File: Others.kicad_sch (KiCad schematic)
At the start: 18 parts, among them J15 UFL, J16 IO1, J17 IO2, Q14 SI2312BDS

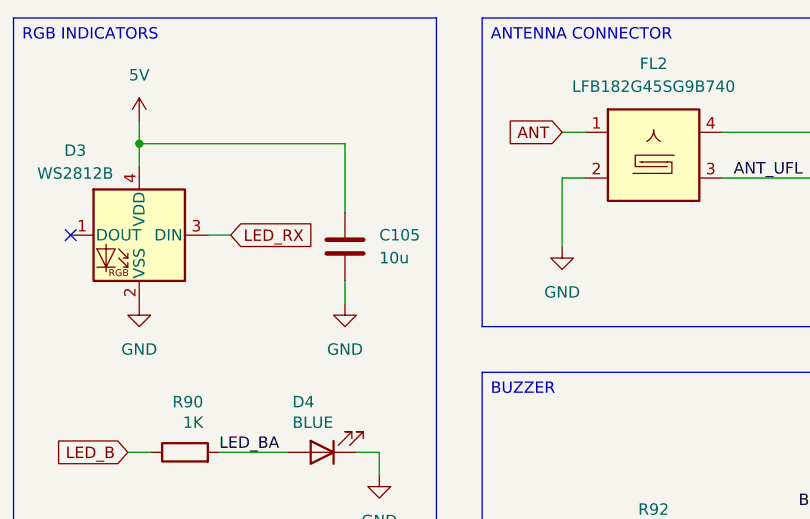
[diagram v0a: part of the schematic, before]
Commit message: Oscillator and IMU layout
Updated the oscillator layout for the RP2350.
Updated the IMU layout for the IMU.
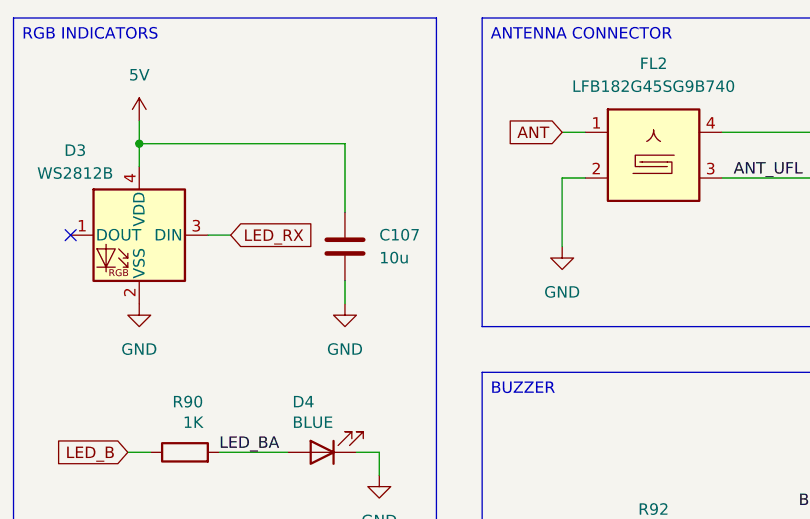
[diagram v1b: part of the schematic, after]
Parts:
- renumbered C105 to C107
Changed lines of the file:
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@@
 		(on_board yes)
 		(dnp no)
-		(property "Reference" "#PWR0216"
+		(property "Reference" "#PWR0217"
 			(at 111.76 96.52 0)
 			(effects
@@
 			(project "ThunderHorse"
 				(path "/ac187c6c-fa53-41cc-bce1-6f39a42a92e8/111cf19a-e0f8-4ba5-b5cb-1102d2b05aed"
-					(reference "#PWR0216")
+					(reference "#PWR0217")
 					(unit 1)
 				)
@@
 		(dnp no)
 		(fields_autoplaced yes)
-		(property "Reference" "#PWR0219"
+		(property "Reference" "#PWR0220"
 			(at 151.13 116.84 0)
 			(effects
@@
 			(project "ThunderHorse"
 				(path "/ac187c6c-fa53-41cc-bce1-6f39a42a92e8/111cf19a-e0f8-4ba5-b5cb-1102d2b05aed"
-					(reference "#PWR0219")
+					(reference "#PWR0220")
 					(unit 1)
 				)
@@
 		(dnp no)
 		(fields_autoplaced yes)
-		(property "Reference" "#PWR0214"
+		(property "Reference" "#PWR0215"
 			(at 85.09 77.47 0)
 			(effects
@@
 			(project "ThunderHorse"
 				(path "/ac187c6c-fa53-41cc-bce1-6f39a42a92e8/111cf19a-e0f8-4ba5-b5cb-1102d2b05aed"
-					(reference "#PWR0214")
+					(reference "#PWR0215")
 					(unit 1)
 				)
@@
 		(dnp no)
 		(fields_autoplaced yes)
-		(property "Reference" "#PWR0222"
+		(property "Reference" "#PWR0223"
 			(at 165.1 71.12 0)
 			(effects
@@
 			(project "ThunderHorse"
 				(path "/ac187c6c-fa53-41cc-bce1-6f39a42a92e8/111cf19a-e0f8-4ba5-b5cb-1102d2b05aed"
-					(reference "#PWR0222")
+					(reference "#PWR0223")
 					(unit 1)
 				)
@@
 		(dnp no)
 		(fields_autoplaced yes)
-		(property "Reference" "#PWR0228"
+		(property "Reference" "#PWR0229"
 			(at 217.17 57.15 0)
 			(effects
@@
 			(project "ThunderHorse"
 				(path "/ac187c6c-fa53-41cc-bce1-6f39a42a92e8/111cf19a-e0f8-4ba5-b5cb-1102d2b05aed"
-					(reference "#PWR0228")
+					(reference "#PWR0229")
 					(unit 1)
 				)
@@
 		(on_board yes)
 		(dnp no)
-		(property "Reference" "#PWR0217"
+		(property "Reference" "#PWR0218"
 			(at 111.76 114.3 0)
 			(effects
@@
 			(project "ThunderHorse"
 				(path "/ac187c6c-fa53-41cc-bce1-6f39a42a92e8/111cf19a-e0f8-4ba5-b5cb-1102d2b05aed"
-					(reference "#PWR0217")
+					(reference "#PWR0218")
 					(unit 1)
 				)
@@
 		(dnp no)
 		(fields_autoplaced yes)
-		(property "Reference" "#PWR0218"
+		(property "Reference" "#PWR0219"
 			(at 132.08 71.12 0)
 			(effects
@@
 			(project "ThunderHorse"
 				(path "/ac187c6c-fa53-41cc-bce1-6f39a42a92e8/111cf19a-e0f8-4ba5-b5cb-1102d2b05aed"
-					(reference "#PWR0218")
+					(reference "#PWR0219")
 					(unit 1)
 				)
@@
 		(on_board yes)
 		(dnp no)
-		(property "Reference" "#PWR0213"
+		(property "Reference" "#PWR0214"
 			(at 85.09 54.61 0)
 			(effects
@@
 			(project "ThunderHorse"
 				(path "/ac187c6c-fa53-41cc-bce1-6f39a42a92e8/111cf19a-e0f8-4ba5-b5cb-1102d2b05aed"
-					(reference "#PWR0213")
+					(reference "#PWR0214")
 					(unit 1)
 				)
@@
 		(dnp no)
 		(fields_autoplaced yes)
-		(property "Reference" "#PWR0223"
+		(property "Reference" "#PWR0224"
 			(at 173.99 71.12 0)
 			(effects
@@
 			(project "ThunderHorse"
 				(path "/ac187c6c-fa53-41cc-bce1-6f39a42a92e8/111cf19a-e0f8-4ba5-b5cb-1102d2b05aed"
-					(reference "#PWR0223")
+					(reference "#PWR0224")
 					(unit 1)
 				)
@@
 		(dnp no)
 		(fields_autoplaced yes)
-		(property "Reference" "#PWR0215"
+		(property "Reference" "#PWR0216"
 			(at 107.95 77.47 0)
 			(effects
@@
 			(project "ThunderHorse"
 				(path "/ac187c6c-fa53-41cc-bce1-6f39a42a92e8/111cf19a-e0f8-4ba5-b5cb-1102d2b05aed"
-					(reference "#PWR0215")
+					(reference "#PWR0216")
 					(unit 1)
 				)
@@
 		(dnp no)
 		(fields_autoplaced yes)
-		(property "Reference" "#PWR0226"
+		(property "Reference" "#PWR0227"
 			(at 213.36 92.71 0)
 			(effects
@@
 			(project "ThunderHorse"
 				(path "/ac187c6c-fa53-41cc-bce1-6f39a42a92e8/111cf19a-e0f8-4ba5-b5cb-1102d2b05aed"
-					(reference "#PWR0226")
+					(reference "#PWR0227")
 					(unit 1)
 				)
@@
 		(dnp no)
 		(fields_autoplaced yes)
-		(property "Reference" "#PWR0220"
+		(property "Reference" "#PWR0221"
 			(at 161.29 91.44 0)
 			(effects
@@
 			(project "ThunderHorse"
 				(path "/ac187c6c-fa53-41cc-bce1-6f39a42a92e8/111cf19a-e0f8-4ba5-b5cb-1102d2b05aed"
-					(reference "#PWR0220")
+					(reference "#PWR0221")
 					(unit 1)
 				)
@@
 		(dnp no)
 		(fields_autoplaced yes)
-		(property "Reference" "#PWR0229"
+		(property "Reference" "#PWR0230"
 			(at 217.17 92.71 0)
 			(effects
@@
 			(project "ThunderHorse"
 				(path "/ac187c6c-fa53-41cc-bce1-6f39a42a92e8/111cf19a-e0f8-4ba5-b5cb-1102d2b05aed"
-					(reference "#PWR0229")
+					(reference "#PWR0230")
 					(unit 1)
 				)
@@
 		(dnp no)
 		(fields_autoplaced yes)
-		(property "Reference" "C105"
+		(property "Reference" "C107"
 			(at 111.76 63.4999 0)
 			(effects
@@
 			(project "ThunderHorse"
 				(path "/ac187c6c-fa53-41cc-bce1-6f39a42a92e8/111cf19a-e0f8-4ba5-b5cb-1102d2b05aed"
-					(reference "C105")
+					(reference "C107")
 					(unit 1)
 				)
@@
 		(dnp no)
 		(fields_autoplaced yes)
-		(property "Reference" "#PWR0221"
+		(property "Reference" "#PWR0222"
 			(at 161.29 116.84 0)
 			(effects
@@
 			(project "ThunderHorse"
 				(path "/ac187c6c-fa53-41cc-bce1-6f39a42a92e8/111cf19a-e0f8-4ba5-b5cb-1102d2b05aed"
-					(reference "#PWR0221")
+					(reference "#PWR0222")
 					(unit 1)
 				)
@@
 		(dnp no)
 		(fields_autoplaced yes)
-		(property "Reference" "#PWR0227"
+		(property "Reference" "#PWR0228"
 			(at 213.36 113.03 0)
 			(effects
@@
 			(project "ThunderHorse"
 				(path "/ac187c6c-fa53-41cc-bce1-6f39a42a92e8/111cf19a-e0f8-4ba5-b5cb-1102d2b05aed"
-					(reference "#PWR0227")
+					(reference "#PWR0228")
 					(unit 1)
 				)
@@
 		(dnp no)
 		(fields_autoplaced yes)
-		(property "Reference" "#PWR0225"
+		(property "Reference" "#PWR0226"
 			(at 213.36 77.47 0)
 			(effects
@@
 			(project "ThunderHorse"
 				(path "/ac187c6c-fa53-41cc-bce1-6f39a42a92e8/111cf19a-e0f8-4ba5-b5cb-1102d2b05aed"
-					(reference "#PWR0225")
+					(reference "#PWR0226")
 					(unit 1)
 				)
@@
 		(dnp no)
 		(fields_autoplaced yes)
-		(property "Reference" "#PWR0224"
+		(property "Reference" "#PWR0225"
 			(at 213.36 57.15 0)
 			(effects
@@
 			(project "ThunderHorse"
 				(path "/ac187c6c-fa53-41cc-bce1-6f39a42a92e8/111cf19a-e0f8-4ba5-b5cb-1102d2b05aed"
-					(reference "#PWR0224")
-					(unit 1)
-				)
+					(reference "#PWR0225")
+					(unit 1)
+				)

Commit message: Power and ESC layout
Updated the power layout.
Updated the ESC layout.

TODO:
Improve track spacing for the ESC.
Complete the power connections.
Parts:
- D4, D5: footprint LED_SMD:LED_0805_2012Metric -> LED_SMD:LED_0603_1608Metric
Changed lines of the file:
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@@
 			)
 		)
-		(property "Footprint" "LED_SMD:LED_0805_2012Metric"
+		(property "Footprint" "LED_SMD:LED_0603_1608Metric"
 			(at 105.41 87.63 0)
 			(effects
@@
 			)
 		)
-		(property "Footprint" "LED_SMD:LED_0805_2012Metric"
+		(property "Footprint" "LED_SMD:LED_0603_1608Metric"
 			(at 105.41 105.41 0)
 			(effects

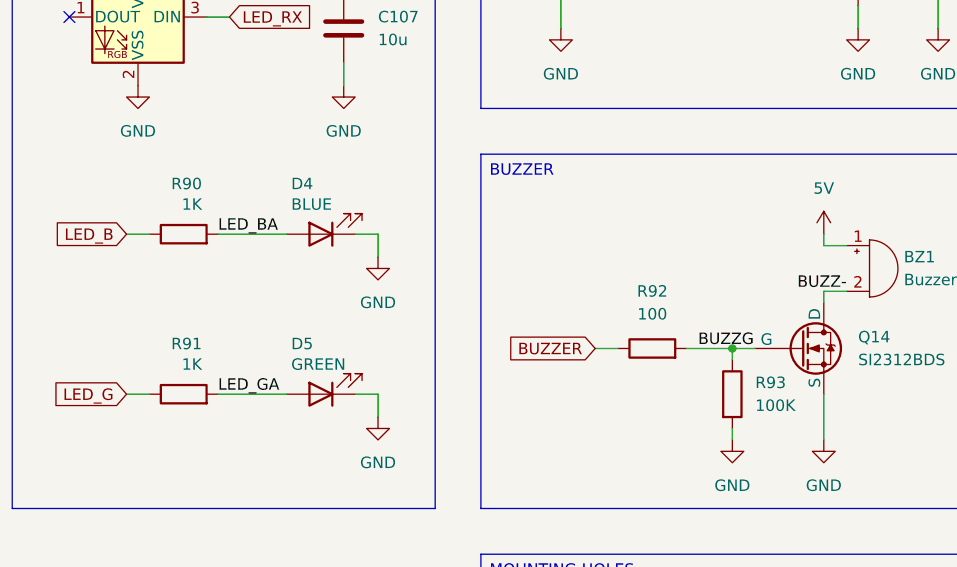
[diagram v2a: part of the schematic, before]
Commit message: Voltage detection
Added a VBUS voltage detection for the RP.
Minor layout changes.
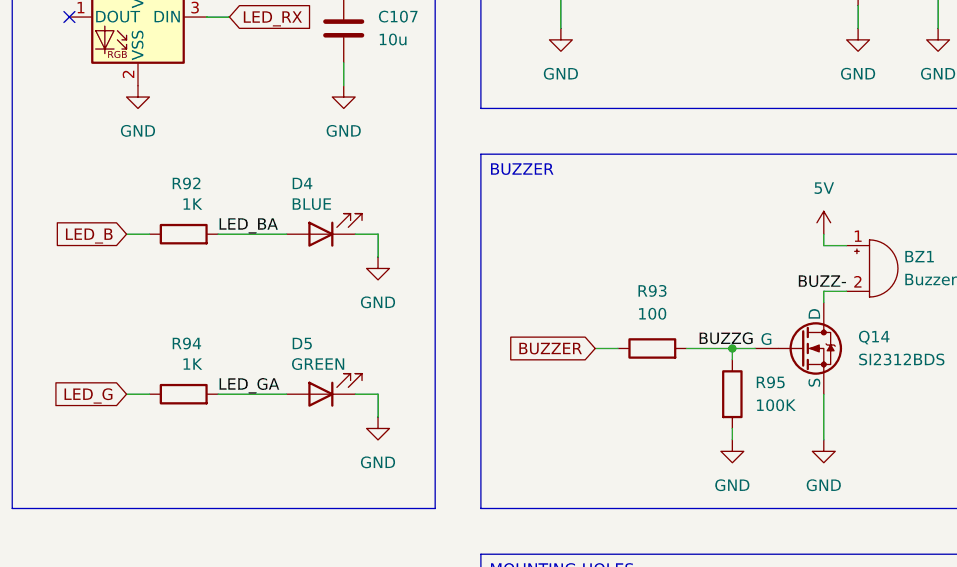
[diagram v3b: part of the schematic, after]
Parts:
- renumbered R90 to R92, R92 to R93, R91 to R94, R93 to R95
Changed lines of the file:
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@@
 		(on_board yes)
 		(dnp no)
-		(property "Reference" "#PWR0217"
+		(property "Reference" "#PWR0227"
 			(at 111.76 96.52 0)
 			(effects
@@
 			(project "ThunderHorse"
 				(path "/ac187c6c-fa53-41cc-bce1-6f39a42a92e8/111cf19a-e0f8-4ba5-b5cb-1102d2b05aed"
-					(reference "#PWR0217")
+					(reference "#PWR0227")
 					(unit 1)
 				)
@@
 		(dnp no)
 		(fields_autoplaced yes)
-		(property "Reference" "#PWR0220"
+		(property "Reference" "#PWR0230"
 			(at 151.13 116.84 0)
 			(effects
@@
 			(project "ThunderHorse"
 				(path "/ac187c6c-fa53-41cc-bce1-6f39a42a92e8/111cf19a-e0f8-4ba5-b5cb-1102d2b05aed"
-					(reference "#PWR0220")
+					(reference "#PWR0230")
 					(unit 1)
 				)
@@
 		(dnp no)
 		(fields_autoplaced yes)
-		(property "Reference" "#PWR0215"
+		(property "Reference" "#PWR0221"
 			(at 85.09 77.47 0)
 			(effects
@@
 			(project "ThunderHorse"
 				(path "/ac187c6c-fa53-41cc-bce1-6f39a42a92e8/111cf19a-e0f8-4ba5-b5cb-1102d2b05aed"
-					(reference "#PWR0215")
+					(reference "#PWR0221")
 					(unit 1)
 				)
@@
 		(on_board yes)
 		(dnp no)
-		(property "Reference" "R91"
+		(property "Reference" "R94"
 			(at 92.202 99.822 90)
 			(effects
@@
 			(project "ThunderHorse"
 				(path "/ac187c6c-fa53-41cc-bce1-6f39a42a92e8/111cf19a-e0f8-4ba5-b5cb-1102d2b05aed"
-					(reference "R91")
+					(reference "R94")
 					(unit 1)
 				)
@@
 		(dnp no)
 		(fields_autoplaced yes)
-		(property "Reference" "#PWR0223"
+		(property "Reference" "#PWR0219"
 			(at 165.1 71.12 0)
 			(effects
@@
 			(project "ThunderHorse"
 				(path "/ac187c6c-fa53-41cc-bce1-6f39a42a92e8/111cf19a-e0f8-4ba5-b5cb-1102d2b05aed"
-					(reference "#PWR0223")
+					(reference "#PWR0219")
 					(unit 1)
 				)
@@
 		(dnp no)
 		(fields_autoplaced yes)
-		(property "Reference" "#PWR0229"
+		(property "Reference" "#PWR0217"
 			(at 217.17 57.15 0)
 			(effects
@@
 			(project "ThunderHorse"
 				(path "/ac187c6c-fa53-41cc-bce1-6f39a42a92e8/111cf19a-e0f8-4ba5-b5cb-1102d2b05aed"
-					(reference "#PWR0229")
+					(reference "#PWR0217")
 					(unit 1)
 				)
@@
 		(on_board yes)
 		(dnp no)
-		(property "Reference" "#PWR0218"
+		(property "Reference" "#PWR0229"
 			(at 111.76 114.3 0)
 			(effects
@@
 			(project "ThunderHorse"
 				(path "/ac187c6c-fa53-41cc-bce1-6f39a42a92e8/111cf19a-e0f8-4ba5-b5cb-1102d2b05aed"
-					(reference "#PWR0218")
+					(reference "#PWR0229")
 					(unit 1)
 				)
@@
 		(dnp no)
 		(fields_autoplaced yes)
-		(property "Reference" "#PWR0219"
+		(property "Reference" "#PWR0218"
 			(at 132.08 71.12 0)
 			(effects
@@
 			(project "ThunderHorse"
 				(path "/ac187c6c-fa53-41cc-bce1-6f39a42a92e8/111cf19a-e0f8-4ba5-b5cb-1102d2b05aed"
-					(reference "#PWR0219")
+					(reference "#PWR0218")
 					(unit 1)
 				)
@@
 		(on_board yes)
 		(dnp no)
-		(property "Reference" "#PWR0214"
+		(property "Reference" "#PWR0215"
 			(at 85.09 54.61 0)
 			(effects
@@
 			(project "ThunderHorse"
 				(path "/ac187c6c-fa53-41cc-bce1-6f39a42a92e8/111cf19a-e0f8-4ba5-b5cb-1102d2b05aed"
-					(reference "#PWR0214")
+					(reference "#PWR0215")
 					(unit 1)
 				)
@@
 		(dnp no)
 		(fields_autoplaced yes)
-		(property "Reference" "R92"
+		(property "Reference" "R93"
 			(at 142.24 93.98 90)
 			(effects
@@
 			(project "ThunderHorse"
 				(path "/ac187c6c-fa53-41cc-bce1-6f39a42a92e8/111cf19a-e0f8-4ba5-b5cb-1102d2b05aed"
-					(reference "R92")
+					(reference "R93")
 					(unit 1)
 				)
@@
 		(dnp no)
 		(fields_autoplaced yes)
-		(property "Reference" "#PWR0224"
+		(property "Reference" "#PWR0220"
 			(at 173.99 71.12 0)
 			(effects
@@
 			(project "ThunderHorse"
 				(path "/ac187c6c-fa53-41cc-bce1-6f39a42a92e8/111cf19a-e0f8-4ba5-b5cb-1102d2b05aed"
-					(reference "#PWR0224")
+					(reference "#PWR0220")
 					(unit 1)
 				)
@@
 		(dnp no)
 		(fields_autoplaced yes)
-		(property "Reference" "#PWR0216"
+		(property "Reference" "#PWR0222"
 			(at 107.95 77.47 0)
 			(effects
@@
 			(project "ThunderHorse"
 				(path "/ac187c6c-fa53-41cc-bce1-6f39a42a92e8/111cf19a-e0f8-4ba5-b5cb-1102d2b05aed"
-					(reference "#PWR0216")
+					(reference "#PWR0222")
 					(unit 1)
 				)
@@
 		(dnp no)
 		(fields_autoplaced yes)
-		(property "Reference" "#PWR0227"
+		(property "Reference" "#PWR0225"
 			(at 213.36 92.71 0)
 			(effects
@@
 			(project "ThunderHorse"
 				(path "/ac187c6c-fa53-41cc-bce1-6f39a42a92e8/111cf19a-e0f8-4ba5-b5cb-1102d2b05aed"
-					(reference "#PWR0227")
+					(reference "#PWR0225")
 					(unit 1)
 				)
@@
 		(dnp no)
 		(fields_autoplaced yes)
-		(property "Reference" "#PWR0221"
+		(property "Reference" "#PWR0224"
 			(at 161.29 91.44 0)
 			(effects
@@
 			(project "ThunderHorse"
 				(path "/ac187c6c-fa53-41cc-bce1-6f39a42a92e8/111cf19a-e0f8-4ba5-b5cb-1102d2b05aed"
-					(reference "#PWR0221")
+					(reference "#PWR0224")
 					(unit 1)
 				)
@@
 		(on_board yes)
 		(dnp no)
-		(property "Reference" "R90"
+		(property "Reference" "R92"
 			(at 92.202 82.042 90)
 			(effects
@@
 			(project "ThunderHorse"
 				(path "/ac187c6c-fa53-41cc-bce1-6f39a42a92e8/111cf19a-e0f8-4ba5-b5cb-1102d2b05aed"
-					(reference "R90")
+					(reference "R92")
 					(unit 1)
 				)
@@
 		(dnp no)
 		(fields_autoplaced yes)
-		(property "Reference" "R93"
+		(property "Reference" "R95"
 			(at 153.67 104.1399 0)
 			(effects
@@
 			(project "ThunderHorse"
 				(path "/ac187c6c-fa53-41cc-bce1-6f39a42a92e8/111cf19a-e0f8-4ba5-b5cb-1102d2b05aed"
-					(reference "R93")
+					(reference "R95")
 					(unit 1)
 				)
@@
 		(dnp no)
 		(fields_autoplaced yes)
-		(property "Reference" "#PWR0230"
+		(property "Reference" "#PWR0226"
 			(at 217.17 92.71 0)
 			(effects
@@
 			(project "ThunderHorse"
 				(path "/ac187c6c-fa53-41cc-bce1-6f39a42a92e8/111cf19a-e0f8-4ba5-b5cb-1102d2b05aed"
-					(reference "#PWR0230")
+					(reference "#PWR0226")
 					(unit 1)
 				)
@@
 		(dnp no)
 		(fields_autoplaced yes)
-		(property "Reference" "#PWR0222"
+		(property "Reference" "#PWR0231"
 			(at 161.29 116.84 0)
 			(effects
@@
 			(project "ThunderHorse"
 				(path "/ac187c6c-fa53-41cc-bce1-6f39a42a92e8/111cf19a-e0f8-4ba5-b5cb-1102d2b05aed"
-					(reference "#PWR0222")
+					(reference "#PWR0231")
 					(unit 1)
 				)
@@
 		(dnp no)
 		(fields_autoplaced yes)
-		(property "Reference" "#PWR0226"
+		(property "Reference" "#PWR0223"
 			(at 213.36 77.47 0)
 			(effects
@@
 			(project "ThunderHorse"
 				(path "/ac187c6c-fa53-41cc-bce1-6f39a42a92e8/111cf19a-e0f8-4ba5-b5cb-1102d2b05aed"
-					(reference "#PWR0226")
+					(reference "#PWR0223")
 					(unit 1)
 				)
@@
 		(dnp no)
 		(fields_autoplaced yes)
-		(property "Reference" "#PWR0225"
+		(property "Reference" "#PWR0216"
 			(at 213.36 57.15 0)
 			(effects
@@
 			(project "ThunderHorse"
 				(path "/ac187c6c-fa53-41cc-bce1-6f39a42a92e8/111cf19a-e0f8-4ba5-b5cb-1102d2b05aed"
-					(reference "#PWR0225")
-					(unit 1)
-				)
+					(reference "#PWR0216")
+					(unit 1)
+				)
